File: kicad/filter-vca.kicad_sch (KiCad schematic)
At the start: 56 parts, among them J41 Conn_01x03_Male, U10 LM13700, U7 TL074, U8 TL072, U9 LM13700

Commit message: component positioning mostly done
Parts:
- C32, C33, C34, C35, C36, C37, C38, C39, C41, C42, C43, C44: footprint rumblesan-standard-parts:C_Rect_L7.0mm_W3.5mm_P5.00mm -> rumblesan-standard-parts:C_Rect_L7.0mm_W2.5mm_P5.00mm
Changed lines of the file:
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@@
       (effects (font (size 1.27 1.27)) (justify left))
     )
-    (property "Footprint" "rumblesan-standard-parts:C_Rect_L7.0mm_W3.5mm_P5.00mm" (id 2) (at 278.765 29.21 0)
+    (property "Footprint" "rumblesan-standard-parts:C_Rect_L7.0mm_W2.5mm_P5.00mm" (id 2) (at 278.765 29.21 0)
       (effects (font (size 1.27 1.27)) hide)
     )
@@
       (effects (font (size 1.27 1.27)) (justify left))
     )
-    (property "Footprint" "rumblesan-standard-parts:C_Rect_L7.0mm_W3.5mm_P5.00mm" (id 2) (at 290.195 29.21 0)
+    (property "Footprint" "rumblesan-standard-parts:C_Rect_L7.0mm_W2.5mm_P5.00mm" (id 2) (at 290.195 29.21 0)
       (effects (font (size 1.27 1.27)) hide)
     )
@@
       (effects (font (size 1.27 1.27)) (justify left))
     )
-    (property "Footprint" "rumblesan-standard-parts:C_Rect_L7.0mm_W3.5mm_P5.00mm" (id 2) (at 302.895 41.91 0)
+    (property "Footprint" "rumblesan-standard-parts:C_Rect_L7.0mm_W2.5mm_P5.00mm" (id 2) (at 302.895 41.91 0)
       (effects (font (size 1.27 1.27)) hide)
     )
@@
     (property "Reference" "C32" (id 0) (at 106.68 32.2412 90))
     (property "Value" "22pF" (id 1) (at 106.68 34.7781 90))
-    (property "Footprint" "rumblesan-standard-parts:C_Rect_L7.0mm_W3.5mm_P5.00mm" (id 2) (at 105.41 32.385 0)
+    (property "Footprint" "rumblesan-standard-parts:C_Rect_L7.0mm_W2.5mm_P5.00mm" (id 2) (at 105.41 32.385 0)
       (effects (font (size 1.27 1.27)) hide)
     )
@@
       (effects (font (size 1.27 1.27)) (justify left))
     )
-    (property "Footprint" "rumblesan-standard-parts:C_Rect_L7.0mm_W3.5mm_P5.00mm" (id 2) (at 278.765 41.91 0)
+    (property "Footprint" "rumblesan-standard-parts:C_Rect_L7.0mm_W2.5mm_P5.00mm" (id 2) (at 278.765 41.91 0)
       (effects (font (size 1.27 1.27)) hide)
     )
@@
       (effects (font (size 1.27 1.27)) (justify left))
     )
-    (property "Footprint" "rumblesan-standard-parts:C_Rect_L7.0mm_W3.5mm_P5.00mm" (id 2) (at 315.595 29.21 0)
+    (property "Footprint" "rumblesan-standard-parts:C_Rect_L7.0mm_W2.5mm_P5.00mm" (id 2) (at 315.595 29.21 0)
       (effects (font (size 1.27 1.27)) hide)
     )
@@
     (property "Reference" "C35" (id 0) (at 270.51 98.2812 90))
     (property "Value" "220pF" (id 1) (at 270.51 100.8181 90))
-    (property "Footprint" "rumblesan-standard-parts:C_Rect_L7.0mm_W3.5mm_P5.00mm" (id 2) (at 269.24 98.425 0)
+    (property "Footprint" "rumblesan-standard-parts:C_Rect_L7.0mm_W2.5mm_P5.00mm" (id 2) (at 269.24 98.425 0)
       (effects (font (size 1.27 1.27)) hide)
     )
@@
       (effects (font (size 1.27 1.27)) (justify left))
     )
-    (property "Footprint" "rumblesan-standard-parts:C_Rect_L7.0mm_W3.5mm_P5.00mm" (id 2) (at 315.595 41.91 0)
+    (property "Footprint" "rumblesan-standard-parts:C_Rect_L7.0mm_W2.5mm_P5.00mm" (id 2) (at 315.595 41.91 0)
       (effects (font (size 1.27 1.27)) hide)
     )
@@
     (property "Reference" "C33" (id 0) (at 118.11 85.5812 90))
     (property "Value" "22pF" (id 1) (at 118.11 88.1181 90))
-    (property "Footprint" "rumblesan-standard-parts:C_Rect_L7.0mm_W3.5mm_P5.00mm" (id 2) (at 116.84 85.725 0)
+    (property "Footprint" "rumblesan-standard-parts:C_Rect_L7.0mm_W2.5mm_P5.00mm" (id 2) (at 116.84 85.725 0)
       (effects (font (size 1.27 1.27)) hide)
     )
@@
       (effects (font (size 1.27 1.27)) (justify left))
     )
-    (property "Footprint" "rumblesan-standard-parts:C_Rect_L7.0mm_W3.5mm_P5.00mm" (id 2) (at 302.895 29.21 0)
+    (property "Footprint" "rumblesan-standard-parts:C_Rect_L7.0mm_W2.5mm_P5.00mm" (id 2) (at 302.895 29.21 0)
       (effects (font (size 1.27 1.27)) hide)
     )
@@
       (effects (font (size 1.27 1.27)) (justify left))
     )
-    (property "Footprint" "rumblesan-standard-parts:C_Rect_L7.0mm_W3.5mm_P5.00mm" (id 2) (at 290.195 41.91 0)
+    (property "Footprint" "rumblesan-standard-parts:C_Rect_L7.0mm_W2.5mm_P5.00mm" (id 2) (at 290.195 41.91 0)
       (effects (font (size 1.27 1.27)) hide)
     )
@@
     (property "Reference" "C34" (id 0) (at 193.04 98.2812 90))
     (property "Value" "220pF" (id 1) (at 193.04 100.8181 90))
-    (property "Footprint" "rumblesan-standard-parts:C_Rect_L7.0mm_W3.5mm_P5.00mm" (id 2) (at 191.77 98.425 0)
-      (effects (font (size 1.27 1.27)) hide)
-    )
+    (property "Footprint" "rumblesan-standard-parts:C_Rect_L7.0mm_W2.5mm_P5.00mm" (id 2) (at 191.77 98.425 0)
+      (effects (font (size 1.27 1.27)) hide)
+    )

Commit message: Final changes for rev01
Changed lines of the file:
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@@
     (stroke (width 0) (type default) (color 0 0 0 0))
   )
-  (wire (pts (xy 345.44 208.28) (xy 345.44 212.09))
+  (wire (pts (xy 345.44 208.28) (xy 345.44 218.44))
     (stroke (width 0) (type default) (color 0 0 0 0))
   )
@@
     (stroke (width 0) (type default) (color 0 0 0 0))
   )
-  (wire (pts (xy 121.92 171.45) (xy 121.92 173.99))
+  (wire (pts (xy 121.92 171.45) (xy 121.92 186.69))
     (stroke (width 0) (type default) (color 0 0 0 0))
   )
@@
     (effects (font (size 1.27 1.27)) (justify left))
   )
-  (hierarchical_label "I_VCA" (shape input) (at 345.44 212.09 270)
+  (hierarchical_label "I_VCA" (shape input) (at 345.44 218.44 270)
     (effects (font (size 1.27 1.27)) (justify right))
   )
-  (hierarchical_label "I_RES" (shape input) (at 121.92 173.99 270)
+  (hierarchical_label "I_RES" (shape input) (at 121.92 186.69 270)
     (effects (font (size 1.27 1.27)) (justify right))
   )

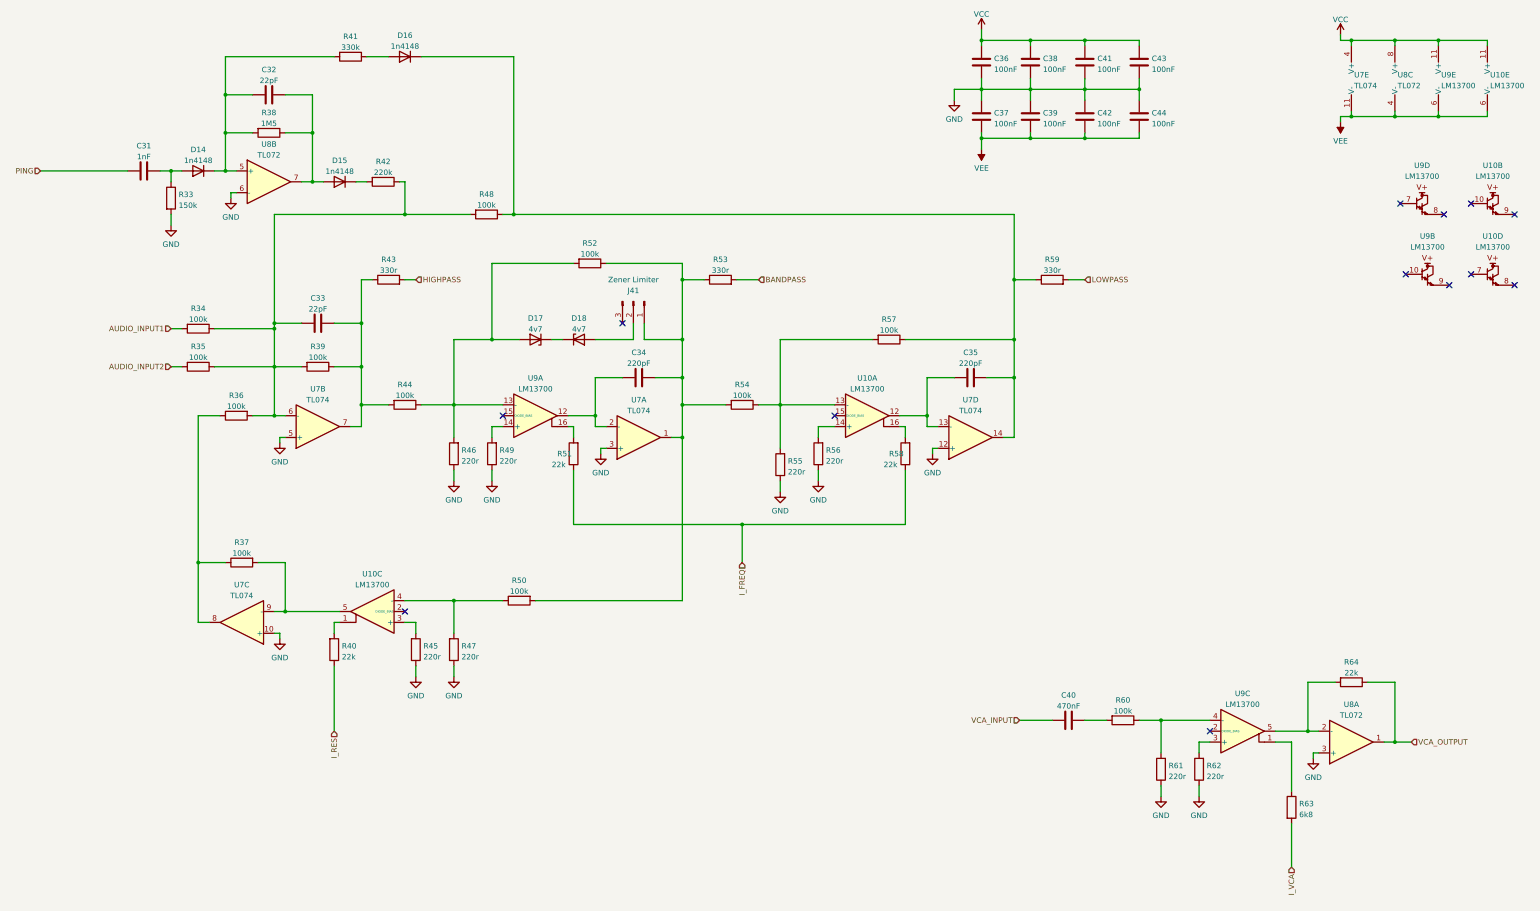
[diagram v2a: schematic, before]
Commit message: Full rejig to use attiny for divider
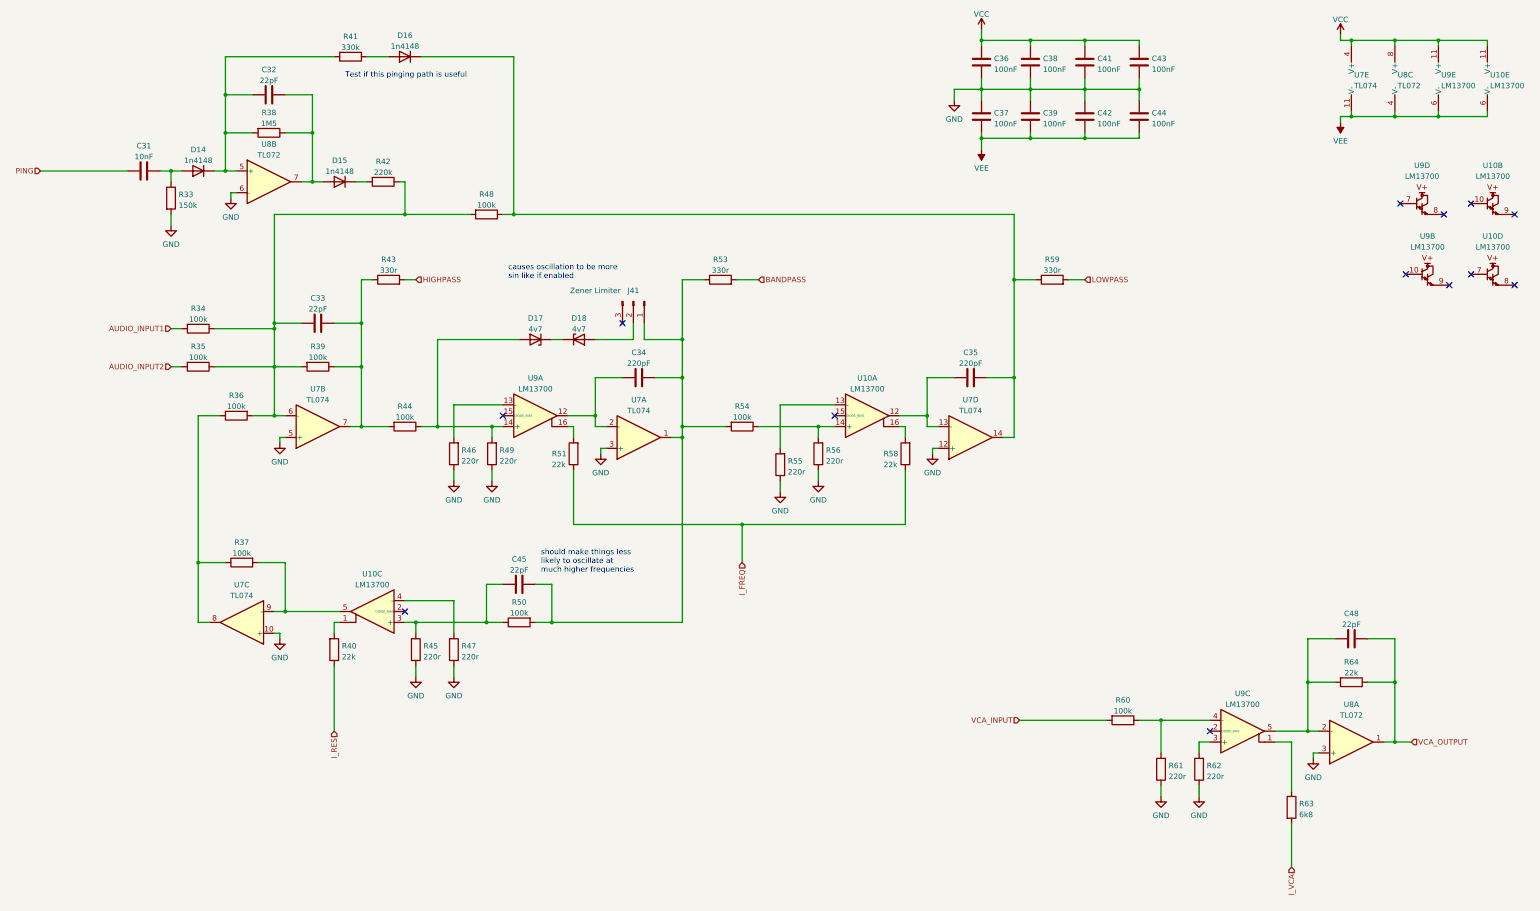
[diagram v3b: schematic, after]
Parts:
- removed C40: 470nF, rumblesan-standard-parts:C_Rect_L7.0mm_W3.5mm_P5.00mm, symbol rumblesan-standard-parts:C
- removed R52, R57: 100k, rumblesan-standard-parts:R_Axial_DIN0207_L6.3mm_D2.5mm_P10.16mm_Horizontal, symbol rumblesan-standard-parts:R
- added C45, C48: 22pF, rumblesan-standard-parts:C_Rect_L7.0mm_W2.5mm_P5.00mm, symbol rumblesan-standard-parts:C
- C31: value 1nF -> 10nF; footprint rumblesan-standard-parts:C_Rect_L7.0mm_W3.5mm_P5.00mm -> rumblesan-standard-parts:C_Rect_L7.0mm_W2.5mm_P5.00mm
- C34, C35: Spec ceramic C0G -> film
- C36, C37, C38, C39, C41, C42, C43, C44: Spec ceramic C0G -> ceramic X7R
- R43, R53, R59: Power (none) -> 0.5W; Spec (none) -> metal film; Tolerance (none) -> 1%
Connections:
- net VCA_INPUT: now also R60.2
- net VCA_OUTPUT: now also C48.2
- net at R64.2, U8.2 (-), U9.5: now also C48.1
- net at C34.2, J41.1 (Pin_1), R50.2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: now also C45.2
- net at D17.2 (A), R44.1: now also R49.2, U9.14 (+); no longer R46.2, U9.13 (-)
- net at R55.2, U10.13 (-): no longer R54.1
- net at R47.2, U10.4 (-): no longer R50.1
- net at R45.2, U10.3 (+): now also R50.1, C45.1
- net at R56.2, U10.14 (+): now also R54.1
- new net: R46.2, U9.13 (-)
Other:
- note added: "Test if this pinging path is useful"
- note added: "causes oscillation to be more sin like if enabled"
- note added: "should make things less likely to oscillate at much higher frequencies"
- moved on the sheet: R44, R50, R54

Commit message: Changing name to the mercurial machine
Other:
- title: (none) -> The Mercurial Machine
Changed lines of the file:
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@@
   (paper "A3")
   (title_block
+    (title "The Mercurial Machine")
+    (date "2023-05-13")
+    (rev "r02")
     (comment 2 "creativecommons.org/licenses/by/4.0/")
     (comment 3 "License: CC BY 4.0")

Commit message: geographically reannotate parts
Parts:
- renumbered C38 to C42, C45 to C43, C39 to C44, C35 to C48, C34 to C49, C37 to C50, C36 to C51, C33 to C52, C41 to C54, C42 to C55, C44 to C56, C48 to C57, C43 to C61, C32 to C64, C31 to C66, D18 to D15, D17 to D16, D16 to D18, D15 to D19, D14 to D22, J41 to J37, R58 to R100, R36 to R101, R39 to R102, R43 to R103, R48 to R104, R37 to R105, R44 to R106, R51 to R107, R62 to R108, R60 to R109, R40 to R111, R42 to R112, R46 to R113, R61 to R117, R64 to R118, R41 to R121, R33 to R124, R38 to R130, R53 to R86, R59 to R87, R50 to R88, R54 to R89, R55 to R90, R56 to R91, R34 to R92, R35 to R93, R45 to R95, R47 to R96, R63 to R97, R49 to R98, U7 to U10, U10 to U12, U9 to U13, U8 to U15

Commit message: Changing name again
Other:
- title: The Mercurial Machine -> Ouroboros
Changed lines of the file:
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@@
   (paper "A3")
   (title_block
-    (title "The Mercurial Machine")
+    (title "Ouroboros")
     (date "2023-05-13")
     (rev "r02")

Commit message: Updating bom and creating part numbers list
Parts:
- C48, C49: Spec film -> film polypropylene
- D15, D16: Spec (none) -> 4.7v zener
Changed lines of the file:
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@@
+      (effects (font (size 1.27 1.27)) hide)
+    )
+    (property "Spec" "4.7v zener" (id 4) (at 179.07 95.25 0)
       (effects (font (size 1.27 1.27)) hide)
     )
@@
     )
     (property "Datasheet" "~" (id 3) (at 168.91 95.25 0)
+      (effects (font (size 1.27 1.27)) hide)
+    )
+    (property "Spec" "4.7v zener" (id 4) (at 168.91 95.25 0)
       (effects (font (size 1.27 1.27)) hide)
     )
@@
       (effects (font (size 1.27 1.27)) hide)
     )
-    (property "Spec" "film" (id 4) (at 270.51 100.33 0)
+    (property "Spec" "film polypropylene" (id 4) (at 270.51 100.33 0)
       (effects (font (size 1.27 1.27)) hide)
     )
@@
       (effects (font (size 1.27 1.27)) hide)
     )
-    (property "Spec" "film" (id 4) (at 193.04 100.33 0)
-      (effects (font (size 1.27 1.27)) hide)
-    )
+    (property "Spec" "film polypropylene" (id 4) (at 193.04 100.33 0)
+      (effects (font (size 1.27 1.27)) hide)
+    )

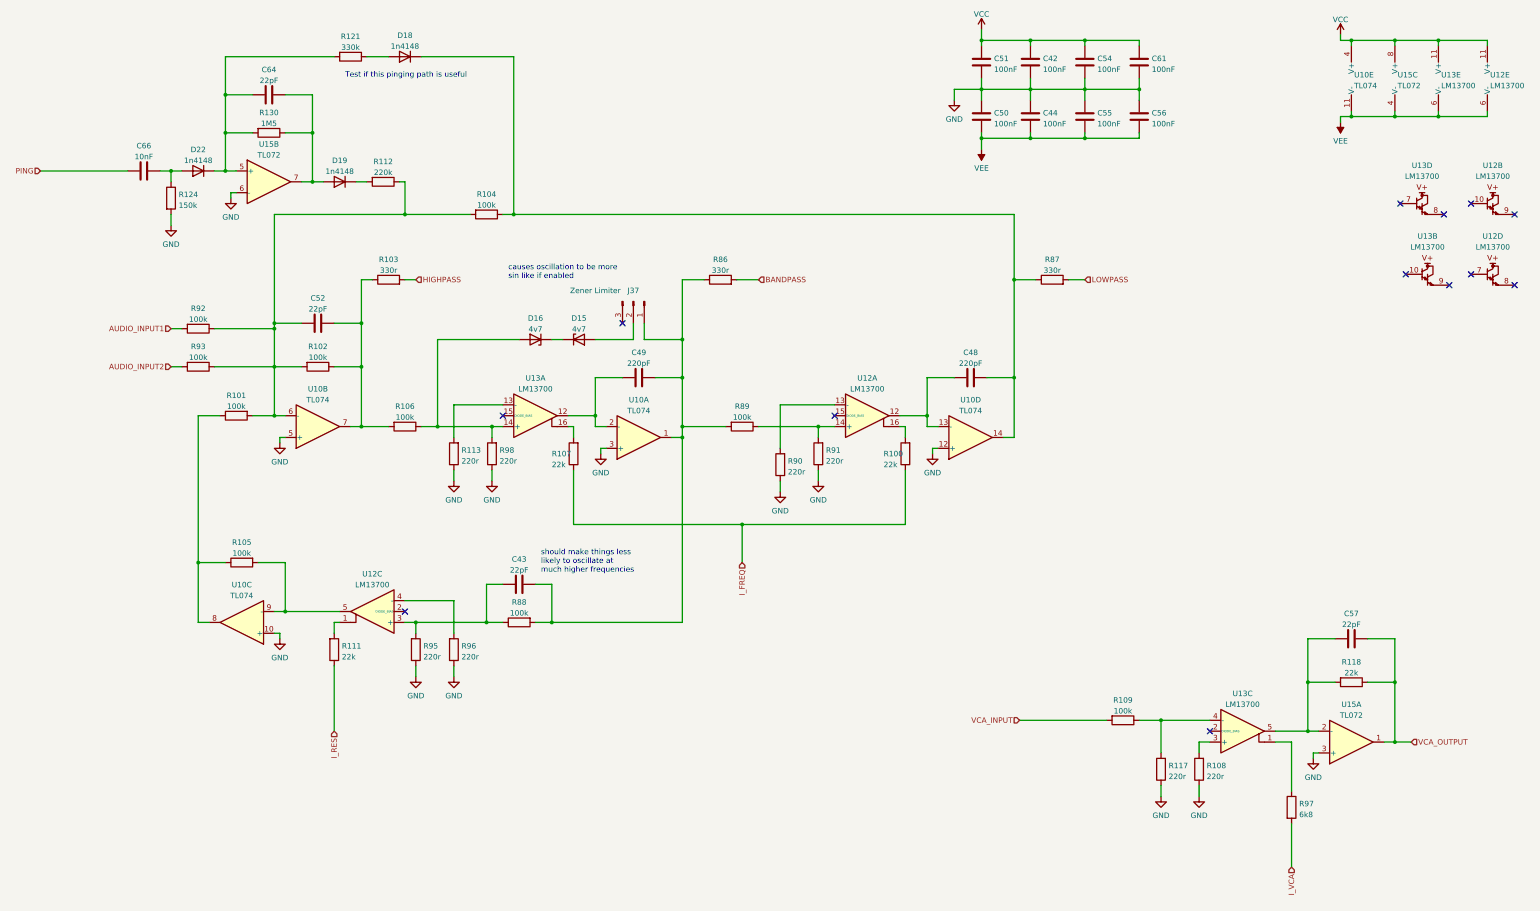
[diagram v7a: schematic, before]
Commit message: Updating for kicad 7
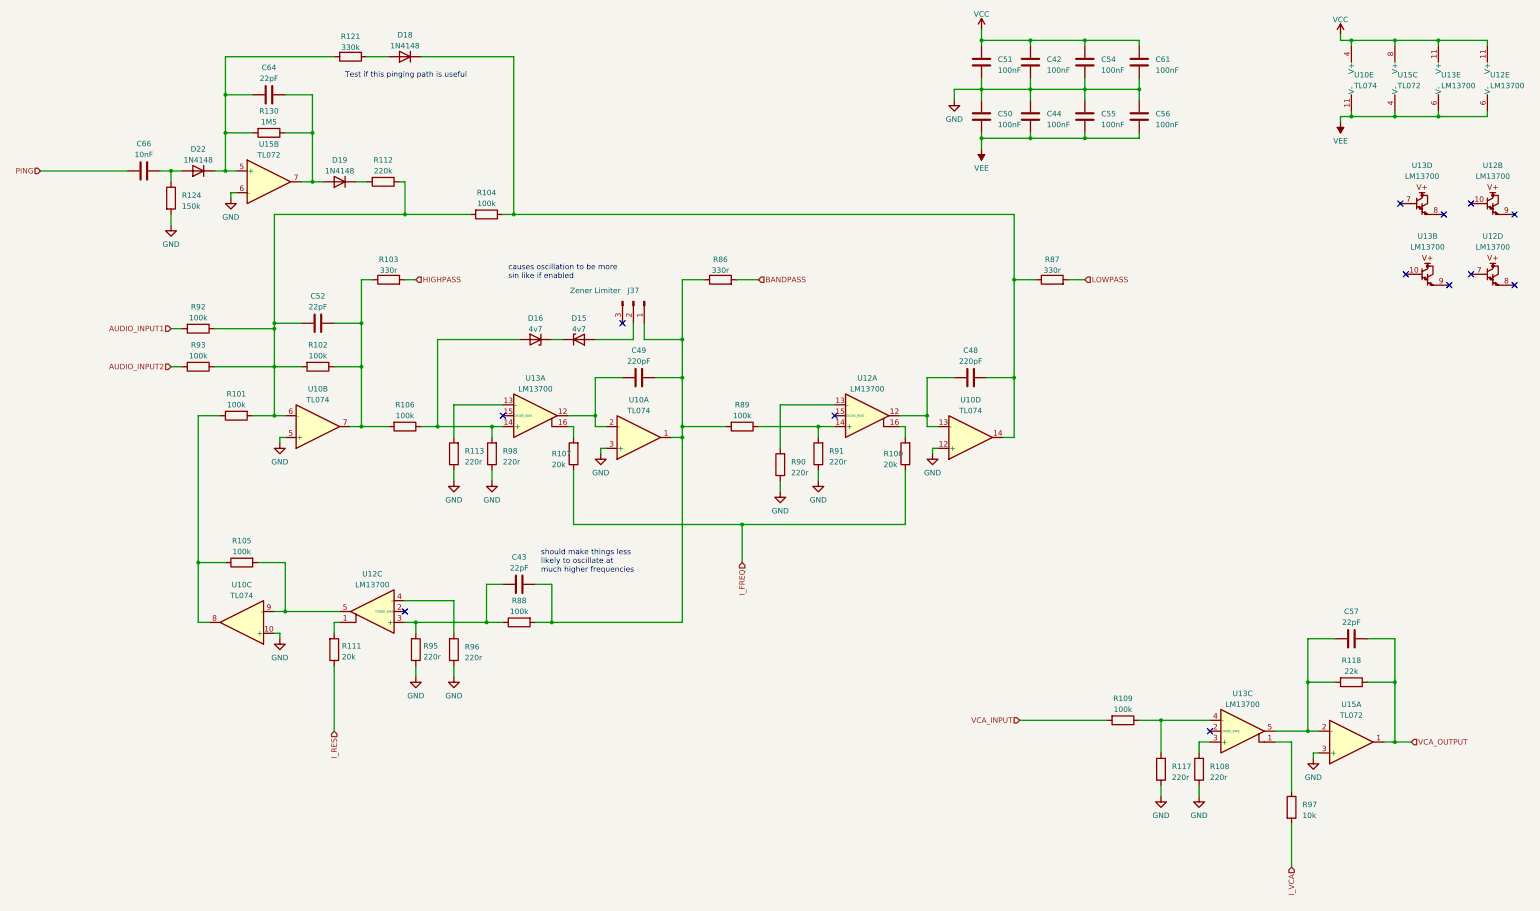
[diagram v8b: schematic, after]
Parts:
- C42, C44, C50, C51, C54, C55, C56, C61: footprint rumblesan-standard-parts:C_Rect_L7.0mm_W2.5mm_P5.00mm -> Rumblesan_Standard_Parts:C_Rect_L7.0mm_W2.5mm_P5.00mm; symbol rumblesan-standard-parts:C -> Rumblesan Standard Parts:C; Spec ceramic X7R -> ceramic C0G
- C43, C48, C49, C52, C57, C64, C66: footprint rumblesan-standard-parts:C_Rect_L7.0mm_W2.5mm_P5.00mm -> Rumblesan_Standard_Parts:C_Rect_L7.0mm_W2.5mm_P5.00mm; symbol rumblesan-standard-parts:C -> Rumblesan Standard Parts:C
- D15, D16: footprint rumblesan-standard-parts:D_DO-35_SOD27_P7.62mm_Horizontal -> Rumblesan_Standard_Parts:D_DO-35_SOD27_P7.62mm_Horizontal
- D18, D19, D22: value 1n4148 -> 1N4148; footprint rumblesan-standard-parts:D_DO-35_SOD27_P7.62mm_Horizontal -> Rumblesan_Standard_Parts:D_DO-35_SOD27_P7.62mm_Horizontal
- J37: symbol Connector:Conn_01x03_Male -> Connector:Conn_01x03_Pin
- R100, R107, R111: value 22k -> 20k; footprint rumblesan-standard-parts:R_Axial_DIN0207_L6.3mm_D2.5mm_P10.16mm_Horizontal -> Rumblesan_Standard_Parts:R_Axial_DIN0207_L6.3mm_D2.5mm_P10.16mm_Horizontal; symbol rumblesan-standard-parts:R -> Rumblesan Standard Parts:R
- R101, R102, R104, R105, R106, R108, R109, R112, R113, R117, R118, R121, R124, R130, R88, R89, R90, R91, R92, R93, R95, R96, R98: footprint rumblesan-standard-parts:R_Axial_DIN0207_L6.3mm_D2.5mm_P10.16mm_Horizontal -> Rumblesan_Standard_Parts:R_Axial_DIN0207_L6.3mm_D2.5mm_P10.16mm_Horizontal; symbol rumblesan-standard-parts:R -> Rumblesan Standard Parts:R
- R103, R86, R87: footprint rumblesan-standard-parts:R_Axial_DIN0207_L6.3mm_D2.5mm_P10.16mm_Horizontal -> Rumblesan_Standard_Parts:R_Axial_DIN0207_L6.3mm_D2.5mm_P10.16mm_Horizontal
- R97: value 6k8 -> 10k; footprint rumblesan-standard-parts:R_Axial_DIN0207_L6.3mm_D2.5mm_P10.16mm_Horizontal -> Rumblesan_Standard_Parts:R_Axial_DIN0207_L6.3mm_D2.5mm_P10.16mm_Horizontal; symbol rumblesan-standard-parts:R -> Rumblesan Standard Parts:R
- U10: footprint rumblesan-standard-parts:DIP-14_W7.62mm_Socket -> Rumblesan_Standard_Parts:DIP-14_W7.62mm_Socket
- U12, U13: footprint rumblesan-standard-parts:DIP-16_W7.62mm_Socket -> Rumblesan_Standard_Parts:DIP-16_W7.62mm_Socket
- U15: footprint rumblesan-standard-parts:DIP-8_W7.62mm_Socket -> Rumblesan_Standard_Parts:DIP-8_W7.62mm_Socket
